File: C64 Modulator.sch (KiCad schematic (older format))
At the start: 29 parts, among them J1 Power, J2 8765, J3 4321, J4 AUD_STEREO, J5 TRS_3.5mm, J6 RCA_PLUG, J7 M_Upper, Q1 BC549, Q2 BC549

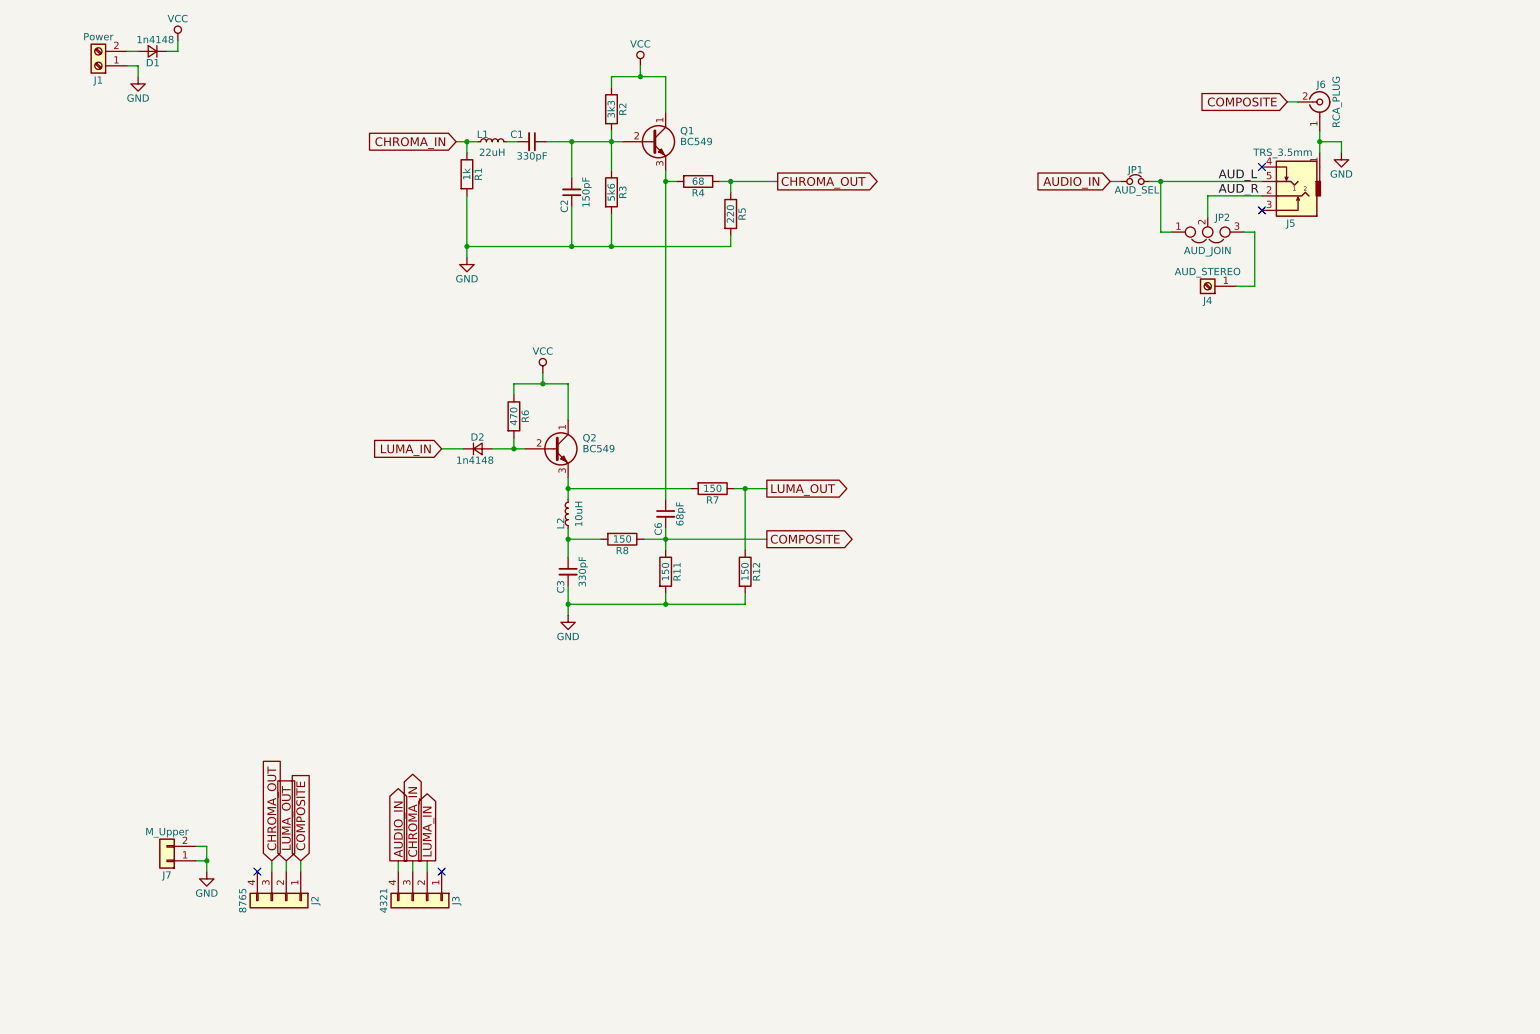
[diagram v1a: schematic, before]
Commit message: Layout and silkscreen done
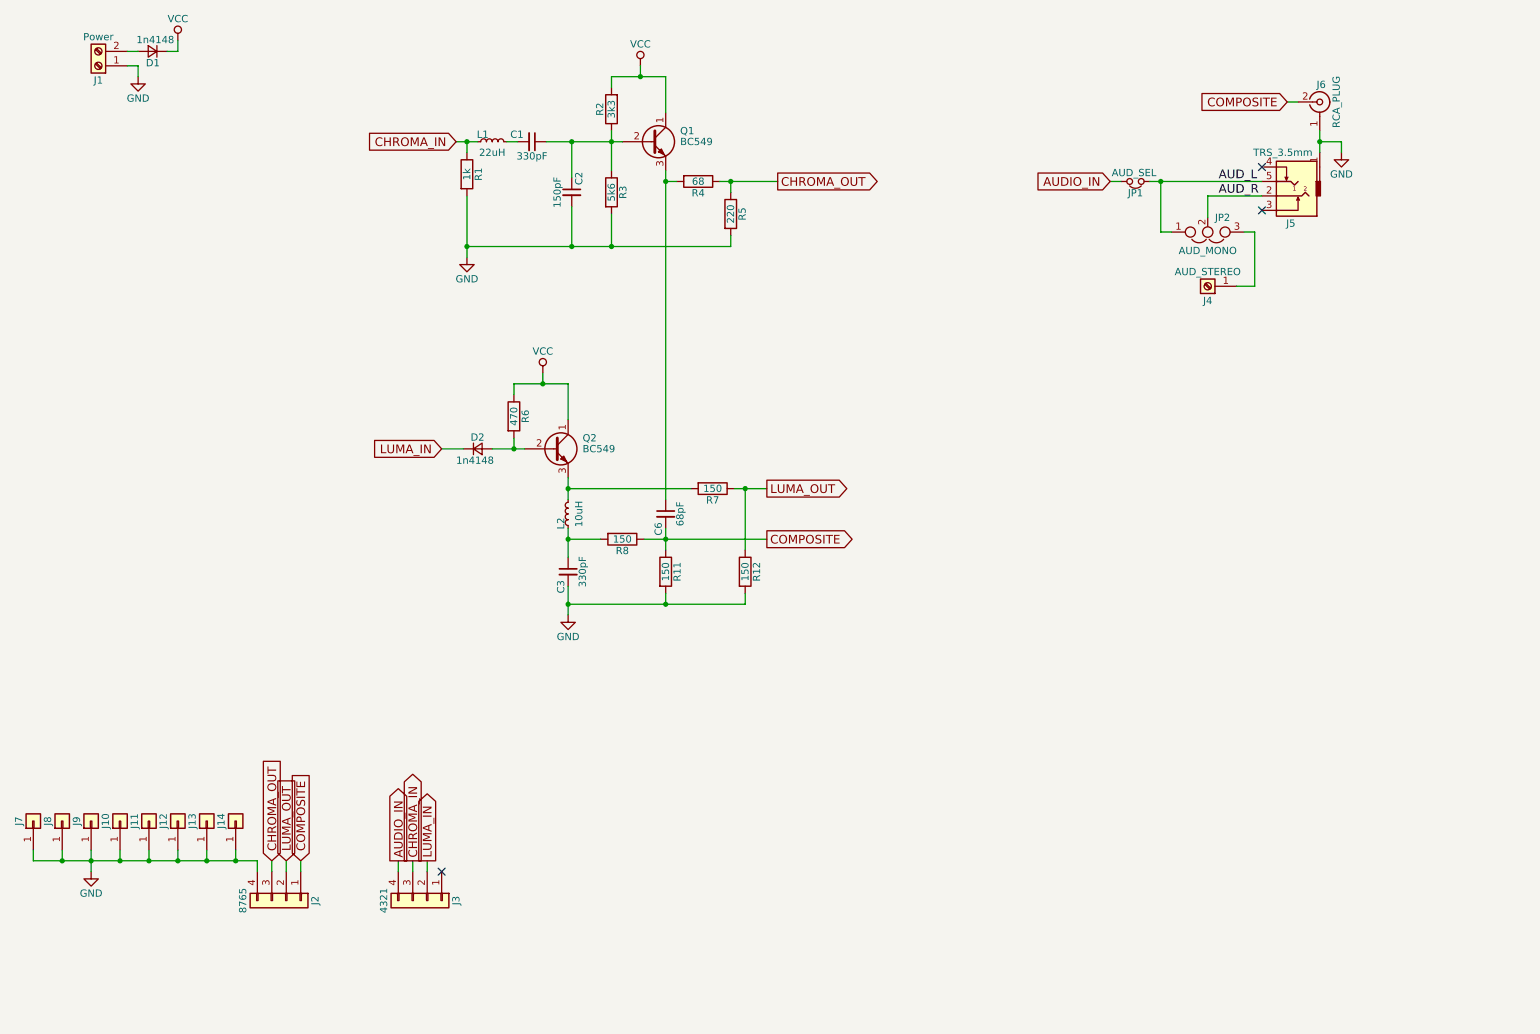
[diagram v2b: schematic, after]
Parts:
- removed J7: M_Upper, Pin_Headers:Pin_Header_Straight_1x02_Pitch2.54mm, symbol Conn_01x02
- added J10, J11, J12, J13, J14, J7, J8, J9: (no value), anchors:anchor_circle, symbol Conn_01x01
- JP2: value AUD_JOIN -> AUD_MONO
- Q1, Q2: footprint TO_SOT_Packages_THT:TO-92_Molded_Narrow -> TO_SOT_Packages_THT:TO-92_Inline_Wide
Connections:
- net AUDIO_IN: now also JP1.2; no longer JP1.1
- net AUD_L: now also JP1.1; no longer JP1.2
- net GND: now also C2.2, J2.4 (Pin_4), J10.1 (Pin_1), J11.1 (Pin_1), J12.1 (Pin_1), J13.1 (Pin_1), J14.1 (Pin_1), J7.1 (Pin_1), J8.1 (Pin_1), J9.1 (Pin_1); no longer C2.1
- net VCC: now also R2.2; no longer R2.1
- net at C1.1, Q1.2 (B), R3.1: now also C2.1, R2.1; no longer C2.2, R2.2
- no-connect marks 4 -> 3
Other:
- moved on the sheet: JP1
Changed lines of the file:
@@
 F 0 "Q1" H 6050 1650 50  0000 L CNN
 F 1 "BC549" H 6050 1575 50  0000 L CNN
-F 2 "TO_SOT_Packages_THT:TO-92_Molded_Narrow" H 6050 1500 50  0001 L CIN
+F 2 "TO_SOT_Packages_THT:TO-92_Inline_Wide" H 6050 1500 50  0001 L CIN
 F 3 "" H 5850 1575 50  0001 L CNN
 	1    5850 1575
@@
 F 3 "" H 5575 1350 50  0001 C CNN
 	1    5575 1350
-	1    0    0    -1
+	-1   0    0    1
 $EndComp
 $Comp
@@
 F 3 "" H 5300 1925 50  0001 C CNN
 	1    5300 1925
-	-1   0    0    1
+	1    0    0    -1
 $EndComp
 Connection ~ 5300 1575
@@
 F 0 "Q2" H 5375 3775 50  0000 L CNN
 F 1 "BC549" H 5375 3700 50  0000 L CNN
-F 2 "TO_SOT_Packages_THT:TO-92_Molded_Narrow" H 5375 3625 50  0001 L CIN
+F 2 "TO_SOT_Packages_THT:TO-92_Inline_Wide" H 5375 3625 50  0001 L CIN
 F 3 "" H 5175 3700 50  0001 L CNN
 	1    5175 3700
@@
 Wire Wire Line
 	3225 6550 3225 6625
-NoConn ~ 3125 6625
 $Comp
 L RCA_PLUG J6
@@
 F 3 "" H 9200 1850 50  0001 C CNN
 	1    9200 1850
-	1    0    0    -1
+	-1   0    0    1
 $EndComp
 Wire Wire Line
@@
 P 9700 2200
 F 0 "JP2" H 9750 2100 50  0000 L CNN
-F 1 "AUD_JOIN" H 9700 2300 50  0000 C BNN
+F 1 "AUD_MONO" H 9700 2300 50  0000 C BNN
 F 2 "Pin_Headers:Pin_Header_Straight_1x03_Pitch2.54mm" H 9700 2200 50  0001 C CNN
 F 3 "" H 9700 2200 50  0001 C CNN
@@
 	10025 2575 9900 2575
 $Comp
-L Conn_01x02 J7
-U 1 1 5D0E39F8
-P 2500 6550
-F 0 "J7" H 2500 6650 50  0000 C CNN
-F 1 "M_Upper" H 2500 6350 50  0000 C CNN
-F 2 "Pin_Headers:Pin_Header_Straight_1x02_Pitch2.54mm" H 2500 6550 50  0001 C CNN
-F 3 "" H 2500 6550 50  0001 C CNN
-	1    2500 6550
-	-1   0    0    1
-$EndComp
-$Comp
 L GND #PWR08
 U 1 1 5D0E3D58
-P 2775 6625
-F 0 "#PWR08" H 2775 6375 50  0001 C CNN
-F 1 "GND" H 2775 6475 50  0000 C CNN
-F 2 "" H 2775 6625 50  0001 C CNN
-F 3 "" H 2775 6625 50  0001 C CNN
-	1    2775 6625
-	1    0    0    -1
-$EndComp
-Wire Wire Line
-	2700 6550 2775 6550
-Wire Wire Line
-	2775 6450 2775 6625
-Wire Wire Line
-	2775 6450 2700 6450
+P 1975 6625
+F 0 "#PWR08" H 1975 6375 50  0001 C CNN
+F 1 "GND" H 1975 6475 50  0000 C CNN
+F 2 "" H 1975 6625 50  0001 C CNN
+F 3 "" H 1975 6625 50  0001 C CNN
+	1    1975 6625
+	1    0    0    -1
+$EndComp
+Wire Wire Line
+	1575 6550 3125 6550
 Connection ~ 2775 6550
+$Comp
+L Conn_01x01 J9
+U 1 1 5D13434E
+P 1975 6275
+F 0 "J9" H 1975 6375 50  0000 C CNN
+F 1 " " V 1875 6250 50  0001 C CNN
+F 2 "anchors:anchor_circle" H 1975 6275 50  0001 C CNN
+F 3 "" H 1975 6275 50  0001 C CNN
+	1    1975 6275
+	0    -1   -1   0
+$EndComp
+Wire Wire Line
+	3125 6550 3125 6625
+$Comp
+L Conn_01x01 J8
+U 1 1 5D134A37
+P 1775 6275
+F 0 "J8" H 1775 6375 50  0000 C CNN
+F 1 " " V 1675 6250 50  0001 C CNN
+F 2 "anchors:anchor_circle" H 1775 6275 50  0001 C CNN
+F 3 "" H 1775 6275 50  0001 C CNN
+	1    1775 6275
+	0    -1   -1   0
+$EndComp
+$Comp
+L Conn_01x01 J7
+U 1 1 5D134AB1
+P 1575 6275
+F 0 "J7" H 1575 6375 50  0000 C CNN
+F 1 " " V 1475 6250 50  0001 C CNN
+F 2 "anchors:anchor_circle" H 1575 6275 50  0001 C CNN
+F 3 "" H 1575 6275 50  0001 C CNN
+	1    1575 6275
+	0    -1   -1   0
+$EndComp
+Wire Wire Line
+	1575 6550 1575 6475
+Wire Wire Line
+	1775 6475 1775 6550
+Connection ~ 2575 6550
+$Comp
+L Conn_01x01 J10
+U 1 1 5D136252
+P 2175 6275
+F 0 "J10" H 2175 6375 50  0000 C CNN
+F 1 " " V 2075 6250 50  0001 C CNN
+F 2 "anchors:anchor_circle" H 2175 6275 50  0001 C CNN
+F 3 "" H 2175 6275 50  0001 C CNN
+	1    2175 6275
+	0    -1   -1   0
+$EndComp
+Wire Wire Line
+	2175 6475 2175 6550
+Connection ~ 2975 6550
+Connection ~ 2175 6550
+$Comp
+L Conn_01x01 J12
+U 1 1 5D1368FD
+P 2575 6275
+F 0 "J12" H 2575 6375 50  0000 C CNN
+F 1 " " V 2475 6250 50  0001 C CNN
+F 2 "anchors:anchor_circle" H 2575 6275 50  0001 C CNN
+F 3 "" H 2575 6275 50  0001 C CNN
+	1    2575 6275
+	0    -1   -1   0
+$EndComp
+$Comp
+L Conn_01x01 J11
+U 1 1 5D136903
+P 2375 6275
+F 0 "J11" H 2375 6375 50  0000 C CNN
+F 1 " " V 2275 6250 50  0001 C CNN
+F 2 "anchors:anchor_circle" H 2375 6275 50  0001 C CNN
+F 3 "" H 2375 6275 50  0001 C CNN
+	1    2375 6275
+	0    -1   -1   0
+$EndComp
+Wire Wire Line
+	2575 6475 2575 6550
+Connection ~ 1775 6550
+Wire Wire Line
+	2375 6475 2375 6550
+Connection ~ 2375 6550
+$Comp
+L Conn_01x01 J14
+U 1 1 5D13747C
+P 2975 6275
+F 0 "J14" H 2975 6375 50  0000 C CNN
+F 1 " " V 2875 6250 50  0001 C CNN
+F 2 "anchors:anchor_circle" H 2975 6275 50  0001 C CNN
+F 3 "" H 2975 6275 50  0001 C CNN
+	1    2975 6275
+	0    -1   -1   0
+$EndComp
+$Comp
+L Conn_01x01 J13
+U 1 1 5D137482
+P 2775 6275
+F 0 "J13" H 2775 6375 50  0000 C CNN
+F 1 " " V 2675 6250 50  0001 C CNN
+F 2 "anchors:anchor_circle" H 2775 6275 50  0001 C CNN
+F 3 "" H 2775 6275 50  0001 C CNN
+	1    2775 6275
+	0    -1   -1   0
+$EndComp
+Wire Wire Line
+	2975 6475 2975 6550
+Wire Wire Line
+	2775 6475 2775 6550
+Wire Wire Line
+	1975 6475 1975 6625
+Connection ~ 1975 6550
 $EndSCHEMATC
